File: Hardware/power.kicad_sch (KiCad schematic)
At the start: 31 parts, among them IC1 LTC4413EDD#PBF, J3 XT30PW-M, Q6 SSM3K15AMFV,L3F, Q8 DMP3099L, U3 LM66200DRLR, U4 MAX77827AEFD+T, U5 SC4215ASTRT

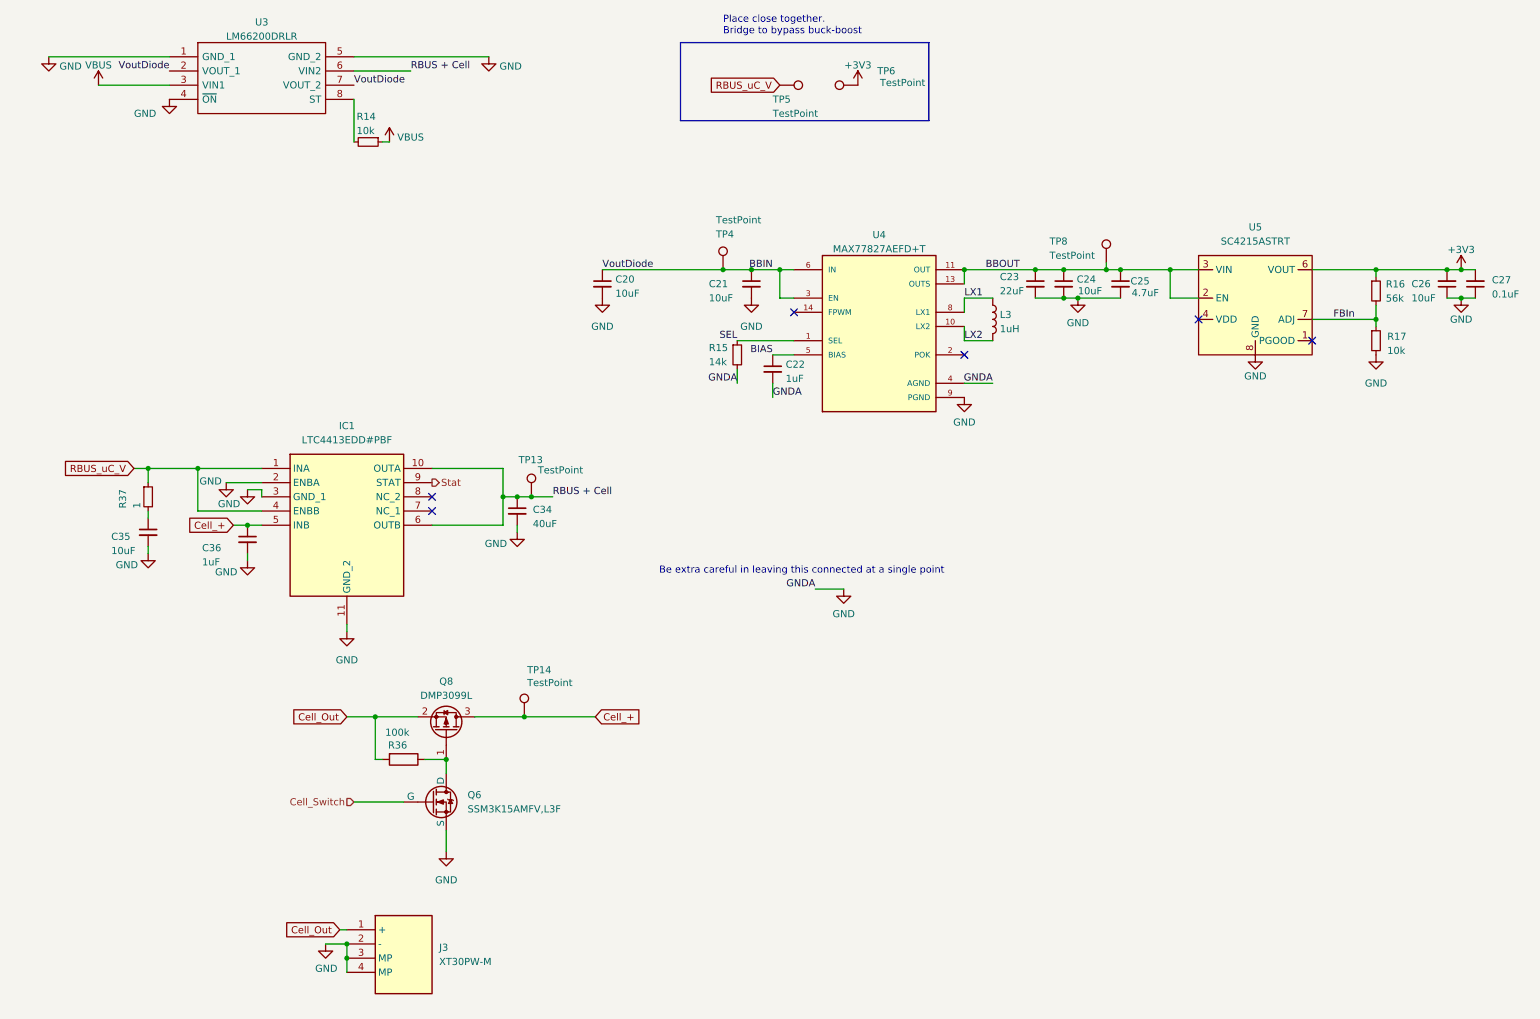
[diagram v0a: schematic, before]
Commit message: GPIO broken out + post review 4
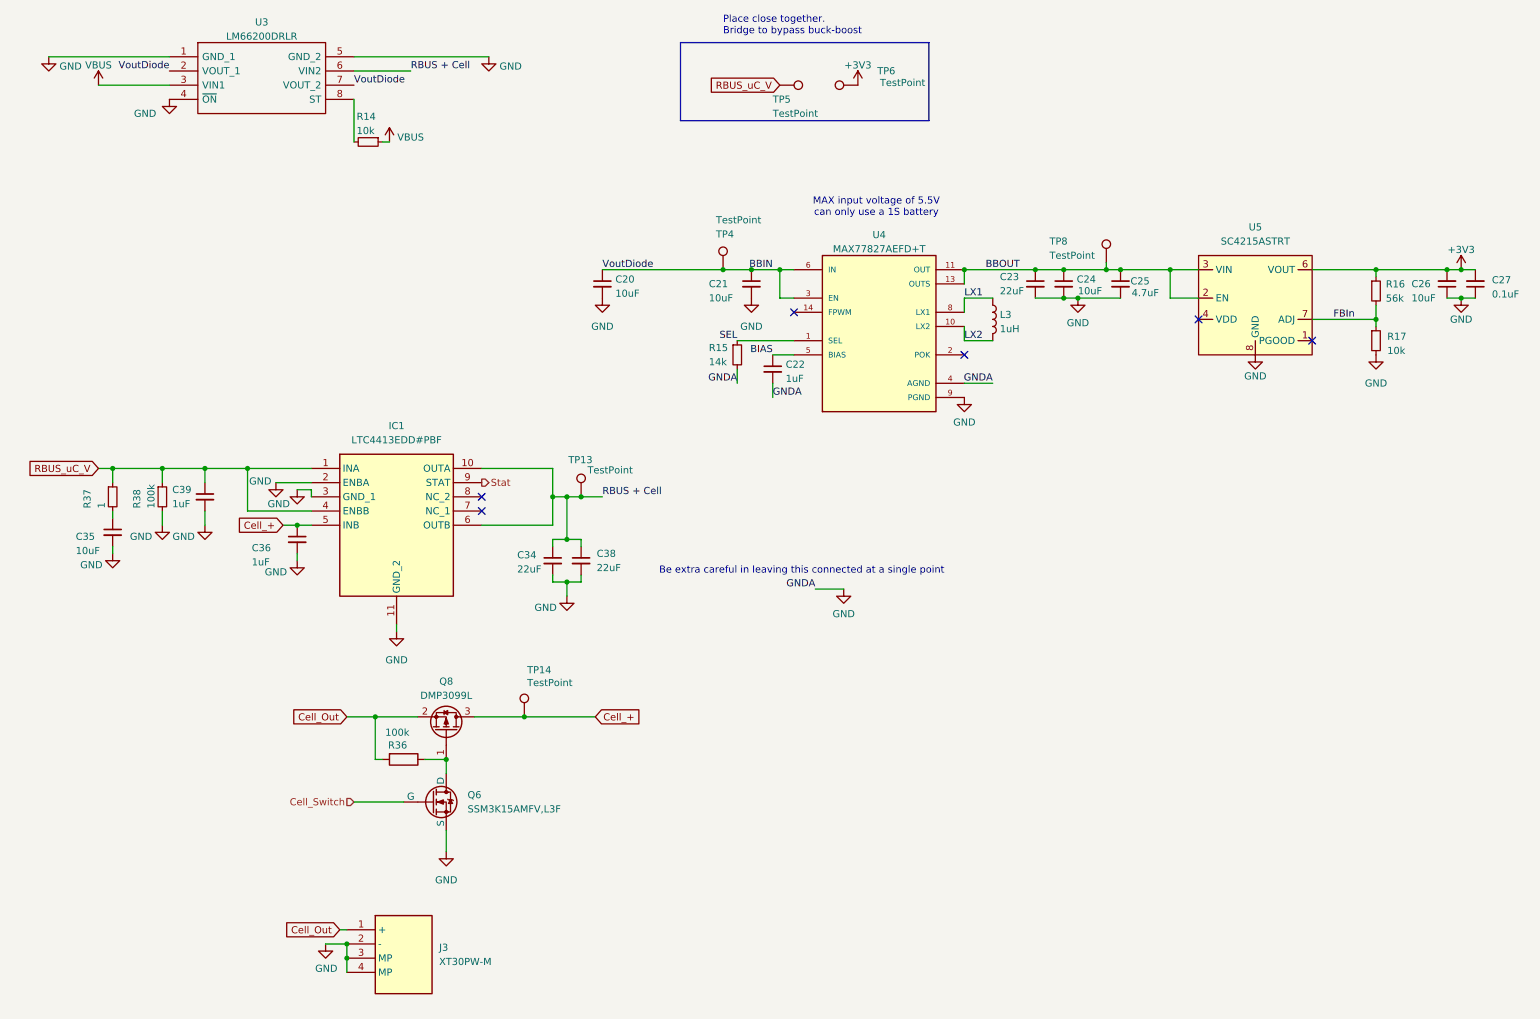
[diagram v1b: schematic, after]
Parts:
- added C38: 22uF, Capacitor_SMD:C_0402_1005Metric, symbol Device:C_Small
- added C39: 1uF, Capacitor_SMD:C_0402_1005Metric, symbol Device:C_Small
- added R38: 100k, Resistor_SMD:R_0402_1005Metric, symbol Device:R_Small
- C34: value 40uF -> 22uF
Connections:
- net GND: now also C38.2, C39.2, R38.2
- net RBUS + Cell: now also C38.1
- net RBUS_uC_V: now also C39.1, R38.1
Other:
- note added: "MAX input voltage of 5.5V can only use a 1S battery"
- moved on the sheet: C34, C35, C36, IC1, R37, TP13

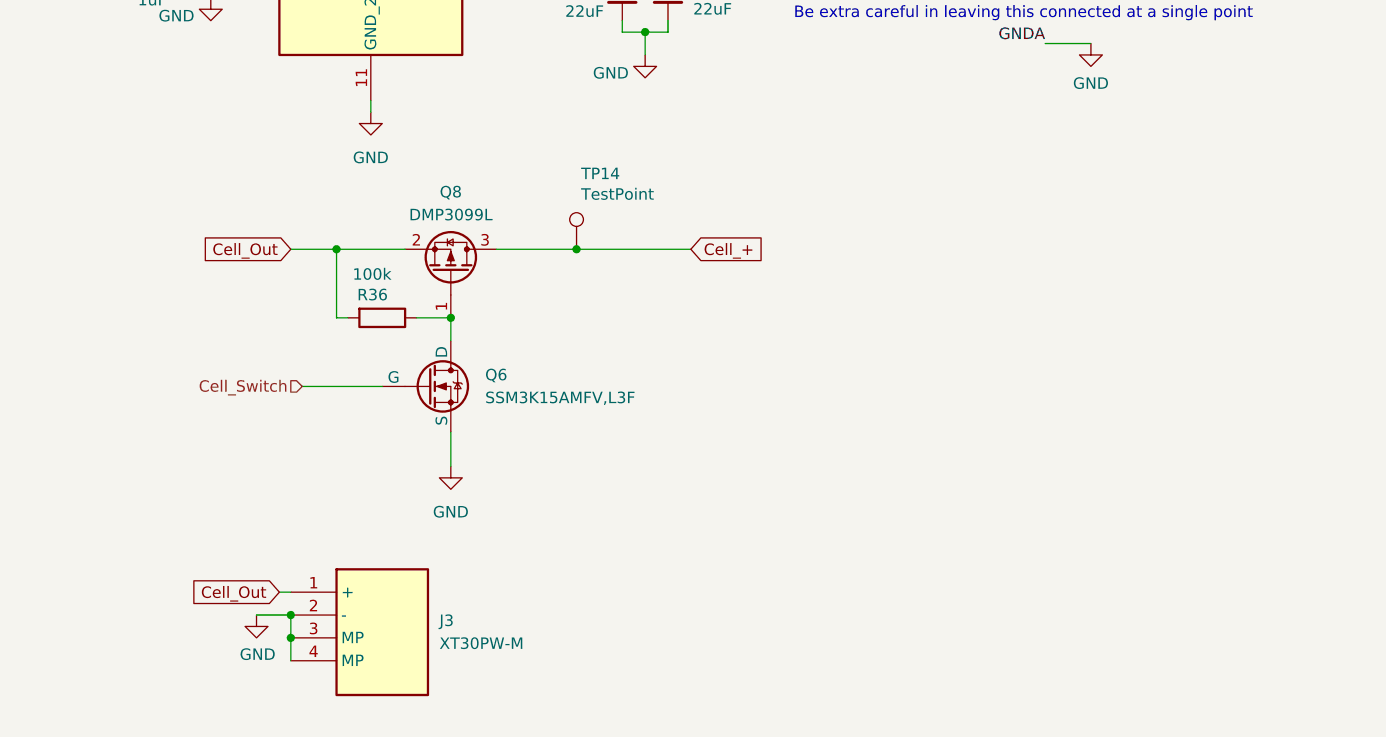
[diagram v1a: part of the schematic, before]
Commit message: Changed mosfet + added top plane for Cell_+ and fixed silkscreen
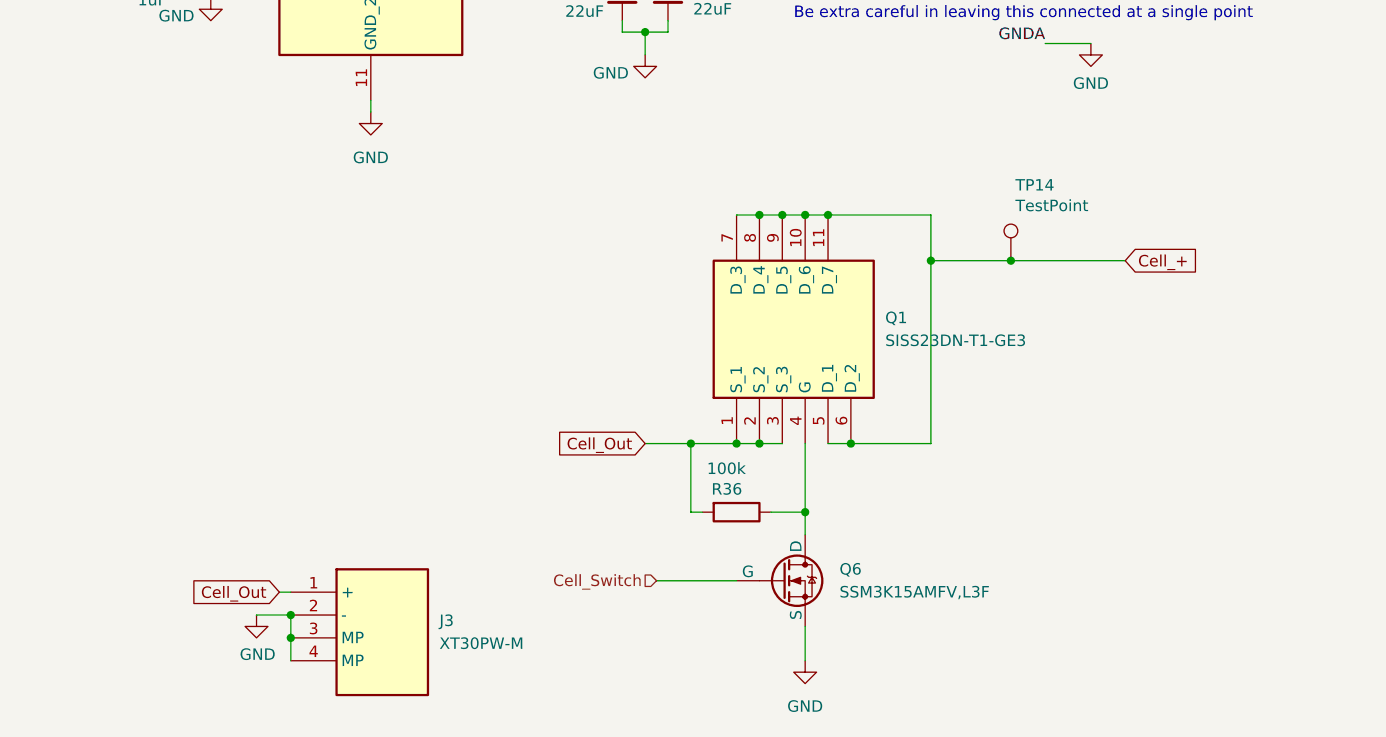
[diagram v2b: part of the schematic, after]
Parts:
- removed Q8: DMP3099L, Package_TO_SOT_SMD:SOT-23, symbol Transistor_FET:DMP3099L
- added Q1: SISS23DN-T1-GE3, iclr:SQS850ENT1_GE3, symbol iclr:SISS23DN-T1-GE3
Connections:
- net Cell_+: now also Q1.10 (D_6), Q1.11 (D_7), Q1.5 (D_1), Q1.6 (D_2), Q1.7 (D_3), Q1.8 (D_4), Q1.9 (D_5)
- net Cell_Out: now also Q1.1 (S_1), Q1.2 (S_2), Q1.3 (S_3)
- net at Q6.1 (D), R36.1: now also Q1.4 (G)
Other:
- moved on the sheet: Q6, R36, TP14

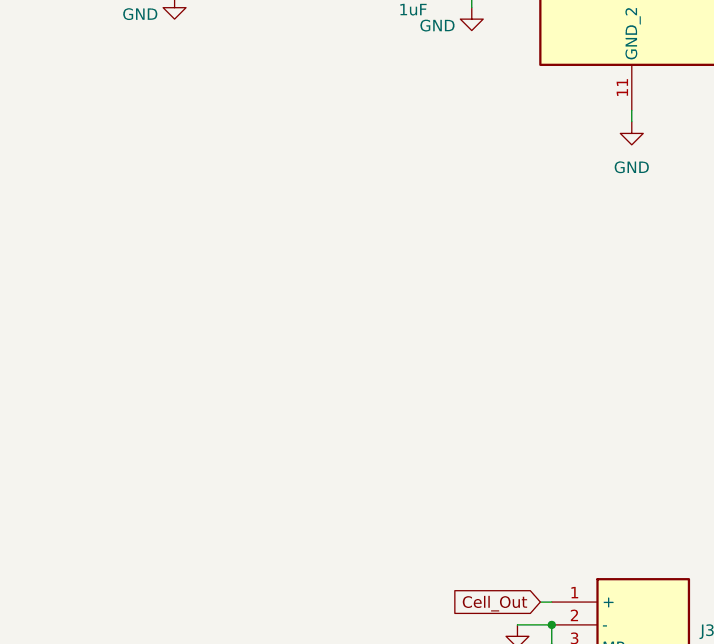
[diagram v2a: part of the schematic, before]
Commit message: Added voltage ref for post ideal diode
(more firmware too)
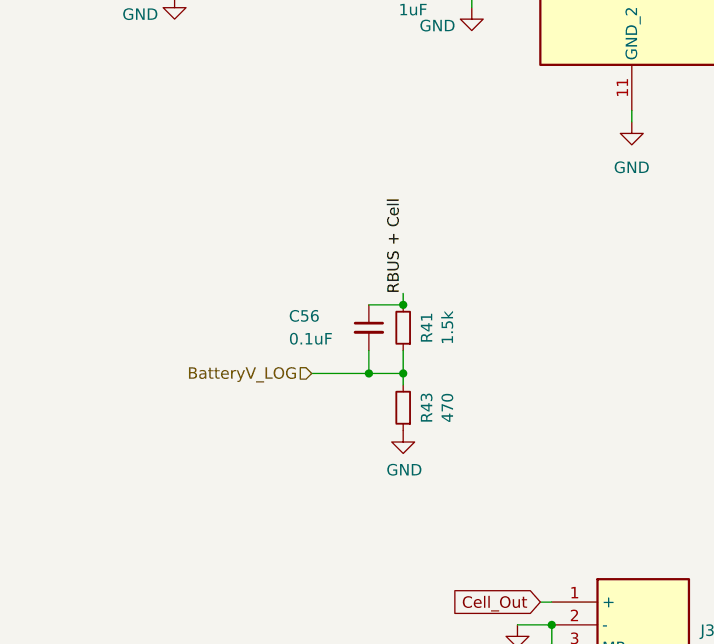
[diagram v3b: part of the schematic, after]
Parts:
- added C56: 0.1uF, Capacitor_SMD:C_0402_1005Metric, symbol Device:C_Small
- added R41: 1.5k, Resistor_SMD:R_0402_1005Metric, symbol Device:R_Small
- added R43: 470, Resistor_SMD:R_0402_1005Metric, symbol Device:R_Small
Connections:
- net GND: now also R43.1
- net RBUS + Cell: now also C56.1, R41.2
- new net BatteryV_LOG: C56.2, R41.1, R43.2

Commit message: Mega commit
Post review changes
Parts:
- removed R43: 470, Resistor_SMD:R_0402_1005Metric, symbol Device:R_Small
- added C57: 0.1uF, Capacitor_SMD:C_0402_1005Metric, symbol Device:C_Small
- added R23, R40: 10k, Resistor_SMD:R_0402_1005Metric, symbol Device:R_Small
- added R24: 1.8k, Resistor_SMD:R_0402_1005Metric, symbol Device:R_Small
- R37: value 1 -> 1R
- R41: value 1.5k -> 18k
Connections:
- net BatteryV_LOG: now also R40.2
- net GND: now also R41.2, R24.2
- net RBUS + Cell: now also R40.1; no longer R41.2
- net Stat renamed ID_Stat
- new net +16.8V: C57.1, R23.1
- new net DeployV_LOG: C57.2, R23.2, R24.1
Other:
- moved on the sheet: C34, C38, Q1, Q6, R36, TP13, TP14

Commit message: Small hardware V2 changes
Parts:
- removed Q6: SSM3K15AMFV,L3F, iclr:SOT-723, symbol Simulation_SPICE:NMOS
- removed R38: 100k, Resistor_SMD:R_0402_1005Metric, symbol Device:R_Small
- added Q5: SSM3K15AMFV,L3F, SSM3K15AMFVL3F, symbol iclr:SSM3K15AMFV,L3F
- added R21: R, symbol Device:R_Small
- added R22: R, Resistor_SMD:R_0402_1005Metric, symbol Device:R_Small
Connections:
- net Cell_Switch: now also Q5.1 (G)
- net GND: now also Q5.2 (S), R22.2
- net RBUS_uC_V: now also R21.1; no longer IC1.4 (ENBB)
- net Cell+_gate: now reaches Q1.4 (G), R36.1
- net Cell+_gate: now also Q5.3 (D)
- new net: IC1.4 (ENBB), R21.2, R22.1
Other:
- note added: "FIX THE IDEAL DIODE WITH POTENTIAL DIVIDER FOR ENBB"
- moved on the sheet: C36

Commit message: V2 changes, PCB finished
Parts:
- Q5: footprint SSM3K15AMFVL3F -> iclr:SSM3K15AMFVL3F
- R21: value R -> 100k; footprint (none) -> Resistor_SMD:R_0402_1005Metric
- R22: value R -> 32k
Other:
- note removed: "FIX THE IDEAL DIODE WITH POTENTIAL DIVIDER FOR ENBB"
- moved on the sheet: C39
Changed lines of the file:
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@@
 		)
 	)
-	(text "FIX THE IDEAL DIODE WITH POTENTIAL DIVIDER FOR ENBB"
-		(exclude_from_sim no)
-		(at 54.61 85.852 0)
-		(effects
-			(font
-				(size 1.27 1.27)
-				(thickness 0.254)
-				(bold yes)
-			)
-		)
-	)
 	(text "Be extra careful in leaving this connected at a single point\n"
 		(exclude_from_sim no)
@@
 	)
 	(junction
-		(at 44.45 97.79)
-		(diameter 0)
-		(color 0 0 0 0)
-	)
-	(junction
 		(at 137.16 62.23)
 		(diameter 0)
@@
 	)
 	(junction
+		(at 40.64 97.79)
+		(diameter 0)
+		(color 0 0 0 0)
+	)
+	(junction
 		(at 53.34 147.32)
 		(diameter 0)
@@
 	(wire
 		(pts
-			(xy 44.45 107.95) (xy 44.45 105.41)
+			(xy 40.64 107.95) (xy 40.64 105.41)
 		)
 		(stroke
@@
 	(wire
 		(pts
-			(xy 44.45 97.79) (xy 50.8 97.79)
-		)
-		(stroke
-			(width 0)
-			(type default)
-		)
-	)
-	(wire
-		(pts
 			(xy 208.28 62.23) (xy 217.17 62.23)
 		)
@@
 	(wire
 		(pts
+			(xy 40.64 97.79) (xy 50.8 97.79)
+		)
+		(stroke
+			(width 0)
+			(type default)
+		)
+	)
+	(wire
+		(pts
 			(xy 114.3 102.87) (xy 114.3 107.95)
 		)
@@
 	(wire
 		(pts
-			(xy 27.94 97.79) (xy 44.45 97.79)
+			(xy 27.94 97.79) (xy 40.64 97.79)
 		)
 		(stroke
@@
 	(wire
 		(pts
-			(xy 44.45 100.33) (xy 44.45 97.79)
+			(xy 40.64 100.33) (xy 40.64 97.79)
 		)
 		(stroke
@@
 			)
 		)
-		(property "Footprint" "SSM3K15AMFVL3F"
+		(property "Footprint" "iclr:SSM3K15AMFVL3F"
 			(at 154.94 265.1 0)
 			(effects
@@
 	(symbol
 		(lib_id "Device:C_Small")
-		(at 44.45 102.87 0)
+		(at 40.64 102.87 0)
 		(unit 1)
 		(exclude_from_sim no)
@@
 		(dnp no)
 		(property "Reference" "C39"
-			(at 38.608 101.6 0)
+			(at 34.798 101.6 0)
 			(effects
 				(font
@@
 		)
 		(property "Value" "1uF"
-			(at 38.608 104.14 0)
+			(at 34.798 104.14 0)
 			(effects
 				(font
@@
 		)
 		(property "Footprint" "Capacitor_SMD:C_0402_1005Metric"
-			(at 44.45 102.87 0)
+			(at 40.64 102.87 0)
 			(effects
 				(font
@@
 		)
 		(property "Datasheet" "~"
-			(at 44.45 102.87 0)
+			(at 40.64 102.87 0)
 			(effects
 				(font
@@
 		)
 		(property "Description" ""
-			(at 44.45 102.87 0)
+			(at 40.64 102.87 0)
 			(effects
 				(font
@@
 		(dnp no)
 		(property "Reference" "R22"
-			(at 46.2579 111.2889 90)
+			(at 52.832 108.204 0)
 			(effects
 				(font
@@
 				)
 				(justify left)
-				(hide yes)
 			)
 		)
-		(property "Value" "R"
-			(at 48.7979 111.2889 90)
+		(property "Value" "32k"
+			(at 53.086 109.982 0)
 			(effects
 				(font
@@
 				)
 				(justify left)
-				(hide yes)
 			)
 		)
@@
 	(symbol
 		(lib_id "power:GND")
-		(at 44.45 107.95 0)
+		(at 40.64 107.95 0)
 		(unit 1)
 		(exclude_from_sim no)
@@
 		(dnp no)
 		(property "Reference" "#PWR089"
-			(at 44.45 114.3 0)
+			(at 40.64 114.3 0)
 			(effects
 				(font
@@
 		)
 		(property "Value" "GND"
-			(at 40.64 109.982 0)
+			(at 36.83 109.982 0)
 			(effects
 				(font
@@
 		)
 		(property "Footprint" ""
-			(at 44.45 107.95 0)
+			(at 40.64 107.95 0)
 			(effects
 				(font
@@
 		)
 		(property "Datasheet" ""
-			(at 44.45 107.95 0)
+			(at 40.64 107.95 0)
 			(effects
 				(font
@@
 		)
 		(property "Description" ""
-			(at 44.45 107.95 0)
+			(at 40.64 107.95 0)
 			(effects
 				(font
@@
 		(dnp no)
 		(property "Reference" "R21"
-			(at 46.2579 103.6689 90)
+			(at 45.466 100.838 0)
 			(effects
 				(font
@@
 				)
 				(justify left)
-				(hide yes)
 			)
 		)
-		(property "Value" "R"
-			(at 48.7979 103.6689 90)
+		(property "Value" "100k"
+			(at 44.45 103.124 0)
 			(effects
 				(font
@@
 				)
 				(justify left)
-				(hide yes)
 			)
 		)
-		(property "Footprint" ""
+		(property "Footprint" "Resistor_SMD:R_0402_1005Metric"
 			(at 50.8 101.6 0)
 			(effects
